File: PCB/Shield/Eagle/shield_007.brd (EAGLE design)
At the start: 101.6 x 53.3 mm, 48 parts, among them IC1 FDB8880, IC2 FDB8880, IC3 FDB8880, IC4 NCV1117ST50T3GOSCT-ND, IC5 NCV1117ST33T3GOSCT-ND

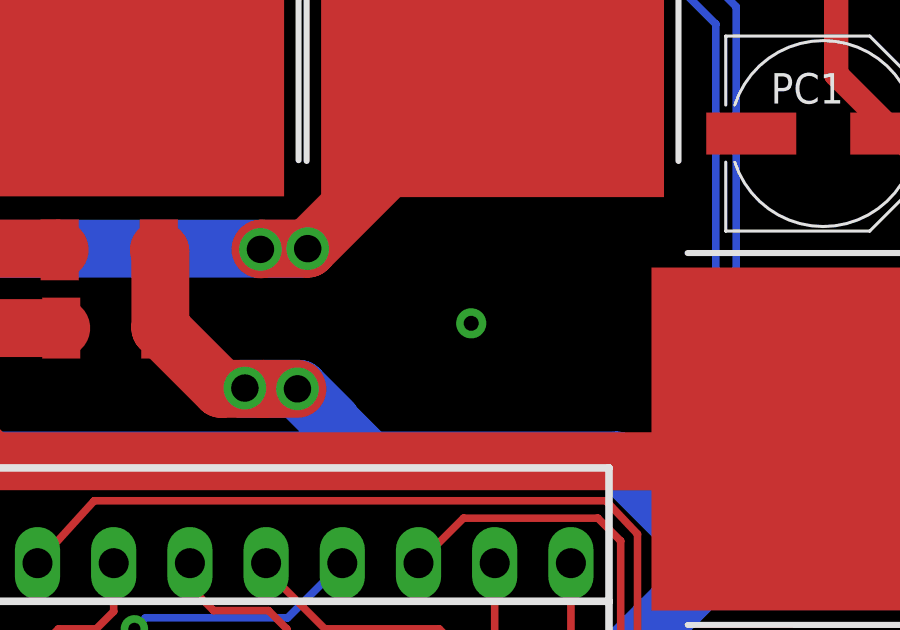
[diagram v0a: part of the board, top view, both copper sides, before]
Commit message: PCB modification, CERN license
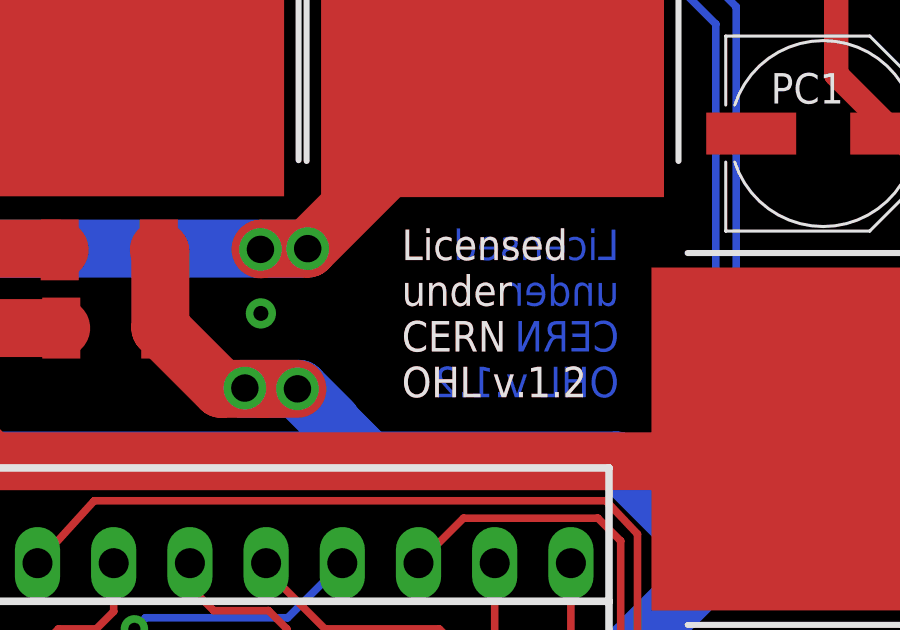
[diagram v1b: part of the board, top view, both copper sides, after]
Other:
- board text added: "Licensed under CERN OHL v.1.2"
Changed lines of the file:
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@@
 <text x="12.7438" y="19.1054" size="1.016" layer="26" ratio="15" rot="MR90">20150923</text>
 <text x="13.6006" y="19.1854" size="1.016" layer="25" ratio="15" rot="R90">20150923</text>
+<text x="51.7144" y="19.1516" size="1.016" layer="16" rot="MR0">Licensed
+under
+CERN
+OHL v.1.2</text>
+<text x="44.4754" y="19.1516" size="1.016" layer="25">Licensed
+under
+CERN
+OHL v.1.2</text>
+<text x="44.4754" y="19.1516" size="1.016" layer="1">Licensed
+under
+CERN
+OHL v.1.2</text>
+<rectangle x1="44.2722" y1="18.796" x2="51.9938" y2="24.9936" layer="41"/>
+<rectangle x1="44.2468" y1="18.7706" x2="52.0192" y2="24.9682" layer="42"/>
 </plain>
 <attributes>
@@
 <via x="62.2554" y="30.226" extent="1-16" drill="0.5" diameter="0.4064" shape="octagon"/>
 <via x="16.4084" y="47.5996" extent="1-16" drill="0.5" diameter="0.4064" shape="octagon"/>
-<via x="46.7868" y="21.6154" extent="1-16" drill="0.5" diameter="0.4064" shape="octagon"/>
+<via x="39.7764" y="21.9456" extent="1-16" drill="0.5" diameter="0.4064" shape="octagon"/>
 <via x="16.0782" y="4.8006" extent="1-16" drill="0.5" diameter="0.4064" shape="octagon"/>
 <via x="73.406" y="11.1506" extent="1-16" drill="0.5" diameter="0.4064" shape="octagon"/>
